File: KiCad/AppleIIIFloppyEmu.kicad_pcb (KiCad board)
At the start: 2 copper layers, 35 x 43 mm, 8 parts, among them J1 Apple III Int/Ext Floppy Port, J2 FloppyEmu / disk ][, J3 Unused

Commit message: Updated README. Update to rev 1.1.
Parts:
- JP1: value ~{EN2} -> ~{DRV2}
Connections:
- net RDDATA renamed RD
- net WRDATA renamed WR
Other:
- board text added: "v1.1"
- board text removed: "v1.0"
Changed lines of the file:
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@@
       (drillshape 0)
       (scaleselection 1)
-      (outputdirectory "Gerber/")
+      (outputdirectory "../Gerber/")
     )
   )
@@
   (net 7 "+5V")
   (net 8 "~{DRIVE1}")
-  (net 9 "RDDATA")
-  (net 10 "WRDATA")
+  (net 9 "RD")
+  (net 10 "WR")
   (net 11 "WPROT")
   (net 12 "~{DRIVE3}")
@@
       (net 19 "+12V") (pinfunction "Pin_15") (pintype "passive"))
     (pad "16" thru_hole circle (at 2.54 17.78) (size 1.7 1.7) (drill 1) (layers *.Cu *.Mask)
-      (net 9 "RDDATA") (pinfunction "Pin_16") (pintype "passive"))
+      (net 9 "RD") (pinfunction "Pin_16") (pintype "passive"))
     (pad "17" thru_hole circle (at 0 20.32) (size 1.7 1.7) (drill 1) (layers *.Cu *.Mask)
       (net 19 "+12V") (pinfunction "Pin_17") (pintype "passive"))
     (pad "18" thru_hole circle (at 2.54 20.32) (size 1.7 1.7) (drill 1) (layers *.Cu *.Mask)
-      (net 10 "WRDATA") (pinfunction "Pin_18") (pintype "passive"))
+      (net 10 "WR") (pinfunction "Pin_18") (pintype "passive"))
     (pad "19" thru_hole circle (at 0 22.86) (size 1.7 1.7) (drill 1) (layers *.Cu *.Mask)
       (net 19 "+12V") (pinfunction "Pin_19") (pintype "passive"))
@@
       (net 23 "/+12V'") (pinfunction "Pin_15") (pintype "passive"))
     (pad "16" thru_hole circle (at 2.54 17.78) (size 1.7 1.7) (drill 1) (layers *.Cu *.Mask)
-      (net 9 "RDDATA") (pinfunction "Pin_16") (pintype "passive"))
+      (net 9 "RD") (pinfunction "Pin_16") (pintype "passive"))
     (pad "17" thru_hole circle (at 0 20.32) (size 1.7 1.7) (drill 1) (layers *.Cu *.Mask)
       (net 23 "/+12V'") (pinfunction "Pin_17") (pintype "passive"))
     (pad "18" thru_hole circle (at 2.54 20.32) (size 1.7 1.7) (drill 1) (layers *.Cu *.Mask)
-      (net 10 "WRDATA") (pinfunction "Pin_18") (pintype "passive"))
+      (net 10 "WR") (pinfunction "Pin_18") (pintype "passive"))
     (pad "19" thru_hole circle (at 0 22.86) (size 1.7 1.7) (drill 1) (layers *.Cu *.Mask)
       (net 23 "/+12V'") (pinfunction "Pin_19") (pintype "passive"))
@@
       (effects (font (size 1 1) (thickness 0.15)) (justify mirror))
     )
-    (fp_text value "~{EN2}" (at -0.1524 2.7686 90) (layer "B.SilkS")
+    (fp_text value "~{DRV2}" (at -0.1524 2.7686 90) (layer "B.SilkS")
       (effects (font (size 0.8 0.8) (thickness 0.1)) (justify mirror))
     )
@@
     (effects (font (size 0.8 0.8) (thickness 0.1)) (justify right mirror))
   )
-  (gr_text "v1.0" (at 140.6398 118.0846) (layer "B.SilkS")
+  (gr_text "v1.1" (at 140.6398 118.0846) (layer "B.SilkS")
     (effects (font (size 0.8 0.8) (thickness 0.1)) (justify mirror))
   )

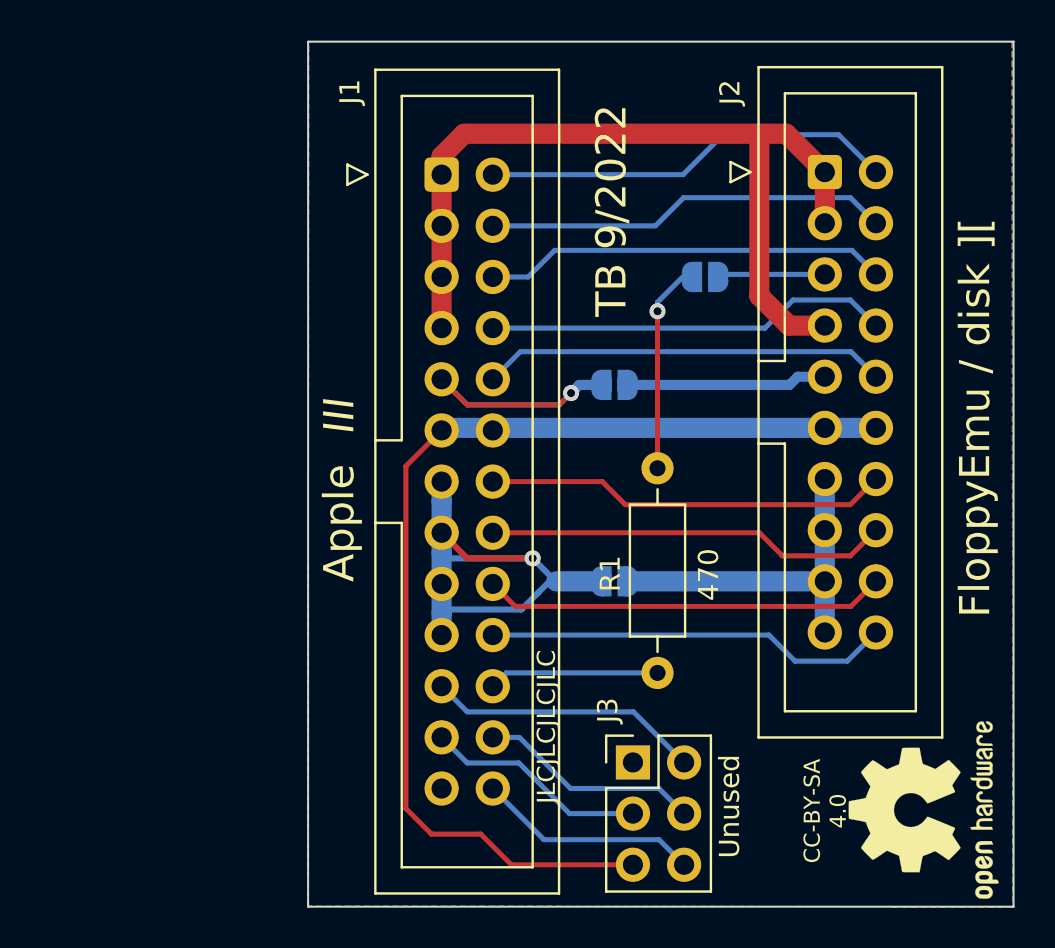
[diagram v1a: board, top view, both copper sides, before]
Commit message: Updated to v2.0: properly handle Apple /// Disk logic when SOS keeps the internal and one external drive spinning concurrently, while alternating the access to both drives. SOS uses this feature when copying volumes: it keeps the internal drive and one of the external drives both spinning, while copying data. This feature is not possible with Apple II drives. However, since Apple /// can enable two drives concurrently, it is necessary to also consider the "INT/EXT" signal. Added a simple OR-gate to combine the DRIVE+INT/EXT singals: both need to be LOW to enable the Apple II drive (or FloppyEmu).
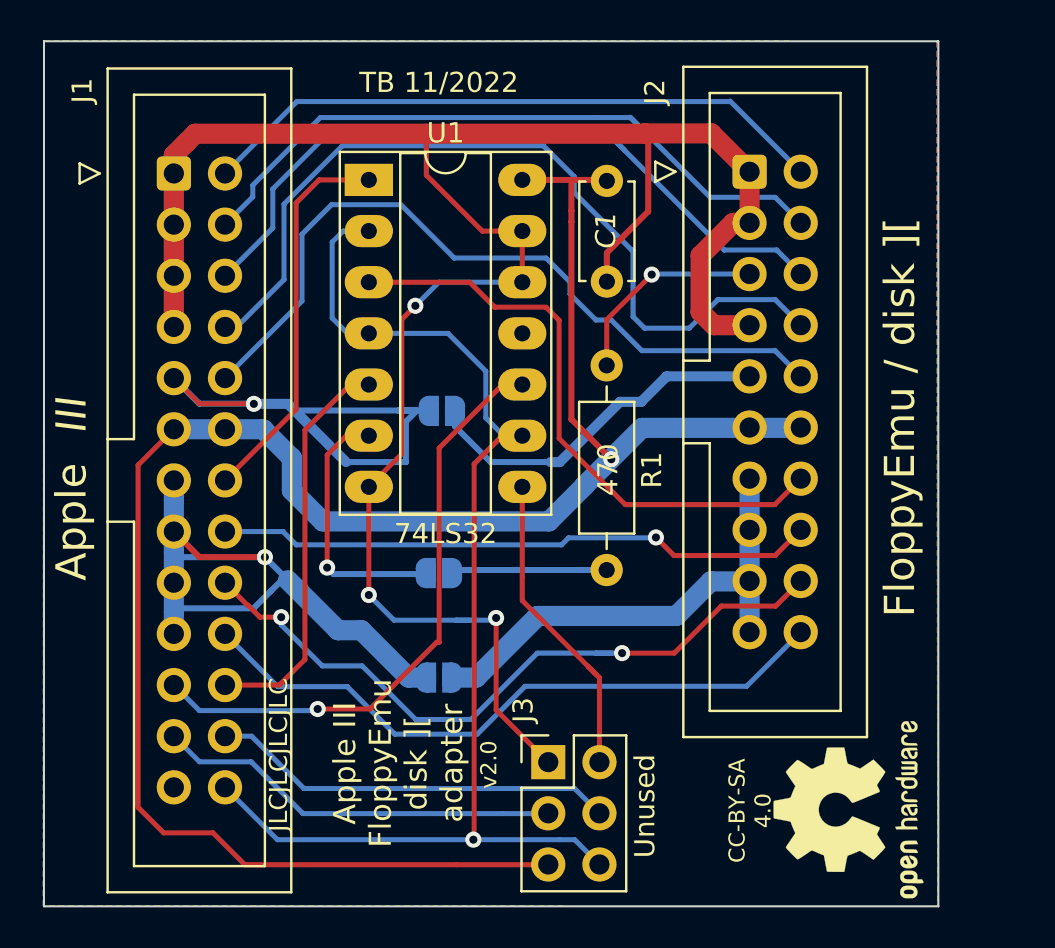
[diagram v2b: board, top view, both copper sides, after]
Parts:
- added C1: 100nF, Capacitor_THT:C_Disc_D4.7mm_W2.5mm_P5.00mm, F.Cu at (128.2, 83.8)
- added U1: 74LS32, Package_DIP:DIP-14_W7.62mm_Socket_LongPads, F.Cu at (116.4, 83.7)
- moved JP1 19.8 mm to (119.9, 103.2)
- moved J1 13.3 mm to (106.7, 83.4)
- moved JP3 9.93 mm to (119.9, 108.4)
- moved JP2 8.67 mm to (120.0, 95.2)
- moved R1 5.70 mm to (128.2, 92.9)
- moved J3 4.20 mm to (125.3, 112.6)
- moved J2 3.73 mm to (135.3, 83.3)
- moved REF*** 3.73 mm to (140.2, 115.0)
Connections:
- net ~{EXT} renamed ~{INT/EXT}
- J1 pad 14: ~{DRIVE1} -> ~{ENABLE1}
- J1 pad 21: ~{DRIVE3} -> ~{ENABLE3}
- J1 pad 22: ~{DRIVE2} -> ~{ENABLE2}
- J2 pad 14: ~{DRIVE1} -> /~{DRIVE1}
- J2 pad 5: /~{DRIVE2'} -> /~{DRIVE2}
- J3 pad 2: ~{DRIVE3} -> /~{DRIVE3}
- JP1 pad 1: /~{DRIVE2'} -> Net-(R1-Pad2)
- JP1 pad 2: Net-(JP1-Pad2) -> Net-(U1-Pad6)
- R1 pad 1: Net-(JP1-Pad2) -> /~{DRIVE2}
- R1 pad 2: ~{DRIVE2} -> Net-(R1-Pad2)
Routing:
- net GND: track 43.3 -> 105.9 mm, vias 0 -> 3
- net ~{INT/EXT}: track 11.1 -> 58.9 mm, vias 0 -> 1
- net +5V: track 53.4 -> 95.9 mm, vias 0 -> 1
- net ~{ENABLE3}: track 0.00 -> 30.4 mm, vias 0 -> 1
- net /~{DRIVE1}: track 0.00 -> 30.0 mm
- net PHASE3: track 20.1 -> 41.8 mm
- net ~{DRIVE1}: track 20.0 -> 0.00 mm
- net ~{ENABLE2}: track 0.00 -> 20.0 mm
- net ~{ENABLE1}: track 0.00 -> 19.3 mm
- net WREQ: track 20.1 -> 38.0 mm
- net PHASE2: track 20.1 -> 37.0 mm
- net /~{DRIVE3}: track 0.00 -> 15.8 mm
- net WR: track 20.0 -> 35.3 mm, vias 0 -> 2
- net PHASE1: track 20.1 -> 34.1 mm
- net ~{DRIVE3}: track 13.6 -> 0.00 mm
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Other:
- board size 35 x 43 mm -> 44.4 x 43 mm
- board text added: "Apple II(I) forever!"
- board text added: "TB 11/2022"
- board text added: "v2.0"
- board text added: "~{ENBL1}"
- board text added: "~{ENBL2}"
- board text added: "~{ENBL3}"
- board text added: "~{INT/EXT}"
- board text removed: "TB 9/2022"
- board text removed: "v1.1"
- board text removed: "~{EXT}"

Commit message: Added optional pull-ups to ENBL1+2 to allow use of 74HCT32 ICs. The pull-ups (R2+R3) are not strictly required for 74LS32 ICs (but recommended anyway). R3 may be soldered on the top side, before soldering the IC socket. Alternatively R3 may be soldered to the bottom side of the PCB (also before soldering the IC socket).
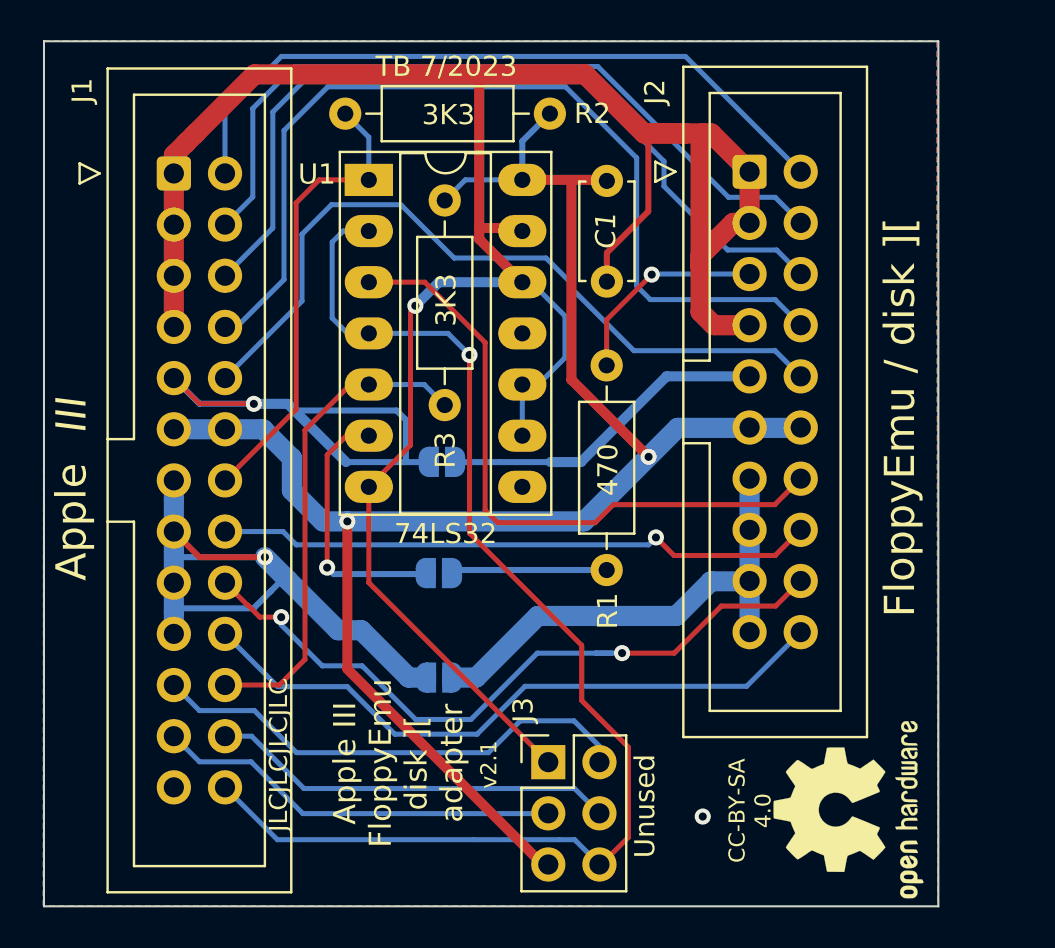
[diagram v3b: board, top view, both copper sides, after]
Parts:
- added R2: 3K3, Resistor_THT:R_Axial_DIN0207_L6.3mm_D2.5mm_P10.16mm_Horizontal, F.Cu at (115.2, 80.4)
- added R3: 3K3, Resistor_THT:R_Axial_DIN0207_L6.3mm_D2.5mm_P10.16mm_Horizontal, F.Cu at (120.2, 94.9)
- moved JP2 2.53 mm to (120.0, 97.7)
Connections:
- J3 pad 2: /~{DRIVE3} -> ~{ENABLE3}
- U1 pad 10: ~{ENABLE3} -> GND
- U1 pad 8: /~{DRIVE3} -> unconnected-(U1-Pad8)
- U1 pad 9: ~{INT/EXT} -> GND
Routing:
- net GND: track 105.9 -> 126.3 mm, vias 3 -> 2
- net /~{DRIVE3}: track 15.8 -> 0.00 mm
- net +5V: track 95.9 -> 84.9 mm, vias 1 -> 2
- net ~{ENABLE3}: track 30.4 -> 24.5 mm, vias 1 -> 0
- net PHASE3: track 41.8 -> 46.5 mm
- net ~{ENABLE2}: track 20.0 -> 24.2 mm
- net ~{INT/EXT}: track 58.9 -> 62.8 mm
- net PHASE2: track 37.0 -> 40.9 mm
- net ~{ENABLE1}: track 19.3 -> 23.1 mm
- net PHASE0: track 31.5 -> 35.1 mm
- net PHASE1: track 34.1 -> 37.6 mm
- net /~{DRIVE1}: track 30.0 -> 32.2 mm
- net /-12V': track 17.9 -> 16.4 mm
- net -12V: track 28.1 -> 27.0 mm
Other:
- board text added: "Apple II(I) Forever!"
- board text added: "TB 7/2023"
- board text added: "v2.1"
- board text removed: "Apple II(I) forever!"
- board text removed: "Set:"
- board text removed: "TB 11/2022"
- board text removed: "v2.0"
- board text removed: "~{DRV3}"
